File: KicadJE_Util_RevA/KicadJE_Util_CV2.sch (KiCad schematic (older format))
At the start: 53 parts, among them J201 SawOut3, J202 SineOut4, Q201 MMBT3906, Q202 UMX1N, SW201 Octave (3 state), U201 TL072, U202 TL072

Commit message: fix flow
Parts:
- added C? (x2): 1u, Capacitor_SMD:C_1206_3216Metric_Pad1.42x1.75mm_HandSolder, symbol Device:C
- added C? (x4): 100n, Capacitor_SMD:C_0805_2012Metric_Pad1.15x1.40mm_HandSolder, symbol Device:C
- added D? (x10): 1N1007, Diode_SMD:D_SOD-123, symbol Device:D
- added D?: LED, LED_SMD:LED_0805_2012Metric_Pad1.15x1.40mm_HandSolder, symbol Device:LED
- added H? (x4): MountingHole_Pad, AJ:MountingHole_Eurorack3, symbol Mechanical:MountingHole_Pad
- added H?: ON, AJ:LED_Hole_3mm, symbol Mechanical:MountingHole
- added J?: In2.1, AJ-Dropbox-Kicad:PJ301SM, symbol Connector:AudioJack2_SwitchT
- added J?: CV2.1, AJ-Dropbox-Kicad:PJ301SM, symbol Connector:AudioJack2_SwitchT
- added J?: Out2.1, AJ-Dropbox-Kicad:PJ301SM, symbol Connector:AudioJack2_SwitchT
- added J?: CV2.2, AJ-Dropbox-Kicad:PJ301SM, symbol Connector:AudioJack2_SwitchT
- added J?: Out2.2, AJ-Dropbox-Kicad:PJ301SM, symbol Connector:AudioJack2_SwitchT
- added J?: In2.2, AJ-Dropbox-Kicad:PJ301SM, symbol Connector:AudioJack2_SwitchT
- added P?: HEADER_2x5_Doepfer, Connector_IDC:IDC-Header_2x05_P2.54mm_Vertical, symbol Eurorack:HEADER_2x5_Doepfer
- added R? (x10): 10k, Resistor_SMD:R_0805_2012Metric_Pad1.15x1.40mm_HandSolder, symbol Device:R
- added R? (x2): 1k, Resistor_SMD:R_0805_2012Metric_Pad1.15x1.40mm_HandSolder, symbol Device:R
- added R?: 22k, Resistor_SMD:R_0805_2012Metric_Pad1.15x1.40mm_HandSolder, symbol Device:R
- added R? (x2): OPEN, Resistor_SMD:R_0805_2012Metric_Pad1.15x1.40mm_HandSolder, symbol Device:R
- added R?: 100k, Resistor_SMD:R_0805_2012Metric_Pad1.15x1.40mm_HandSolder, symbol Device:R
- added RV?: 100k Offset1, AJ-Dropbox-Kicad:Potentiometer_China_RK09_Single_Vertical_AJ, symbol Envelope-cache-2018-08-04-13-00-04:POT
- added TP?: Tri, AJ:Jack_6m3, symbol Connector:TestPoint
- added TP?: SQ, AJ:Jack_6m3, symbol Connector:TestPoint
- added TP?: SS, AJ:Jack_6m3, symbol Connector:TestPoint
- added TP?: In3, AJ:Jack_6m3, symbol Connector:TestPoint
- added TP?: In2, AJ:Jack_6m3, symbol Connector:TestPoint
- added TP?: In1, AJ:Jack_6m3, symbol Connector:TestPoint
- added TP?: OFF1, AJ:Pot_6m3_scale1, symbol Connector:TestPoint
- added U? (x3): TL072, AJ-Dropbox-Kicad:AJ_SO-8_5.3x6.2mm_P1.27mm, symbol Amplifier_Operational:TL072
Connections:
- net labels added: CV2.1, CV2.2, In2.1, In2.2, Out1, Out2.1, Out2.2
- wire segments 170 -> 319
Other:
- note added: "Power"
- moved on the sheet: C201, C202, C203, C204, C205, D201, J201, J202, JP201, Q201, Q202A, Q202B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

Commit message: Glide initiated
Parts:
- removed C201: 220p, Capacitor_SMD:C_0805_2012Metric_Pad1.15x1.40mm_HandSolder, symbol Device:C
- removed C202, C203: 100n, Capacitor_SMD:C_0805_2012Metric_Pad1.15x1.40mm_HandSolder, symbol Device:C
- removed C204: 1n poly, Capacitor_THT:C_Rect_L7.0mm_W2.0mm_P5.00mm, symbol Device:C
- removed C205: 1n alt, Capacitor_SMD:C_0805_2012Metric_Pad1.15x1.40mm_HandSolder, symbol Device:C
- removed D201: Germanium, Diode_THT:D_A-405_P7.62mm_Horizontal, symbol Device:D
- removed D? (x4): 1N1007, Diode_SMD:D_SOD-123, symbol Device:D
- removed J201: SawOut3, AJ-Dropbox-Kicad:PJ301SM, symbol Connector:AudioJack2_SwitchT
- removed J202: SineOut4, AJ-Dropbox-Kicad:PJ301SM, symbol Connector:AudioJack2_SwitchT
- removed JP201: Jumper_3_Bridged12, Jumper:SolderJumper-3_P1.3mm_Bridged12_Pad1.0x1.5mm_NumberLabels, symbol Jumper:Jumper_3_Bridged12
- removed Q201: MMBT3906, Package_TO_SOT_SMD:SOT-23, symbol Transistor_BJT:MMBT3906
- removed Q202: UMX1N, AJ:UMX1N_UMT6_DualNPN, symbol UMX1N:UMX1N
- removed R201, R203, R225: 47k, Resistor_SMD:R_0805_2012Metric_Pad1.15x1.40mm_HandSolder, symbol Device:R
- removed R202, R218, R234: 1k, Resistor_SMD:R_0805_2012Metric_Pad1.15x1.40mm_HandSolder, symbol Device:R
- removed R204: 1k6, Resistor_SMD:R_0805_2012Metric_Pad1.15x1.40mm_HandSolder, symbol Device:R
- removed R206, R213: 12k5, Resistor_SMD:R_0805_2012Metric_Pad1.15x1.40mm_HandSolder, symbol Device:R
- removed R207: 26k7, Resistor_SMD:R_0805_2012Metric_Pad1.15x1.40mm_HandSolder, symbol Device:R
- removed R208: 6k04, Resistor_SMD:R_0805_2012Metric_Pad1.15x1.40mm_HandSolder, symbol Device:R
- removed R209: 1M2, Resistor_SMD:R_0805_2012Metric_Pad1.15x1.40mm_HandSolder, symbol Device:R
- removed R211: 1k82, Resistor_SMD:R_0805_2012Metric_Pad1.15x1.40mm_HandSolder, symbol Device:R
- removed R212, R216, R221, R227, R230, R? (x5): 10k, Resistor_SMD:R_0805_2012Metric_Pad1.15x1.40mm_HandSolder, symbol Device:R
- removed R217: 3k, Resistor_SMD:R_0805_2012Metric_Pad1.15x1.40mm_HandSolder, symbol Device:R
- removed R219, R222: OPEN, Resistor_SMD:R_0805_2012Metric_Pad1.15x1.40mm_HandSolder, symbol Device:R
- removed R220: 15k, Resistor_SMD:R_0805_2012Metric_Pad1.15x1.40mm_HandSolder, symbol Device:R
- removed R223: 0R, Resistor_SMD:R_0805_2012Metric_Pad1.15x1.40mm_HandSolder, symbol Device:R
- removed R224, R?: 100k, Resistor_SMD:R_0805_2012Metric_Pad1.15x1.40mm_HandSolder, symbol Device:R
- removed R226, R231: 2k20, Resistor_SMD:R_0805_2012Metric_Pad1.15x1.40mm_HandSolder, symbol Device:R
- removed R228: 390R, Resistor_SMD:R_0805_2012Metric_Pad1.15x1.40mm_HandSolder, symbol Device:R
- removed R229: 18k, Resistor_SMD:R_0805_2012Metric_Pad1.15x1.40mm_HandSolder, symbol Device:R
- removed R232, R233: 13k3, Resistor_SMD:R_0805_2012Metric_Pad1.15x1.40mm_HandSolder, symbol Device:R
- removed RV201: 5k, Potentiometer_THT:Potentiometer_Bourns_3296W_Vertical, symbol Device:R_POT_TRIM
- removed RV202: 50k, Potentiometer_THT:Potentiometer_Bourns_3296W_Vertical, symbol Device:R_POT_TRIM
- removed RV?: 100k Offset1, AJ-Dropbox-Kicad:Potentiometer_China_RK09_Single_Vertical_AJ, symbol Envelope-cache-2018-08-04-13-00-04:POT
- removed TP201: Saw, AJ:Jack_6m3, symbol Connector:TestPoint
- removed TP203: 3m5 jack, AJ:Jack_6m3, symbol Connector:TestPoint
- removed TP?: OFF1, AJ:Pot_6m3_scale1, symbol Connector:TestPoint
- removed U201, U202, U?: TL072, AJ-Dropbox-Kicad:AJ_SO-8_5.3x6.2mm_P1.27mm, symbol Amplifier_Operational:TL072
- added C? (x2): 100n, Capacitor_SMD:C_0805_2012Metric_Pad1.15x1.40mm_HandSolder, symbol Device:C
- added D? (x2): LED, LED_THT:LED_D3.0mm, symbol Device:LED
- added R? (x5): 20k, Resistor_SMD:R_0805_2012Metric_Pad1.15x1.40mm_HandSolder, symbol Device:R
- added R? (x2): 220R, Resistor_SMD:R_0805_2012Metric_Pad1.15x1.40mm_HandSolder, symbol Device:R
- added R? (x2): OPEN, Resistor_SMD:R_0805_2012Metric_Pad1.15x1.40mm_HandSolder, symbol Device:R
- added R? (x2): 1k, Resistor_SMD:R_0805_2012Metric_Pad1.15x1.40mm_HandSolder, symbol Device:R
- added R?: 10k, Resistor_SMD:R_0805_2012Metric_Pad1.15x1.40mm_HandSolder, symbol Device:R
- added R?: LDR03, OptoDevice:R_LDR_10x8.5mm_P7.6mm_Vertical, symbol Sensor_Optical:LDR03
- added RV?: 100k Glide1, AJ-Dropbox-Kicad:Potentiometer_China_RK09_Single_Vertical_AJ, symbol Envelope-cache-2018-08-04-13-00-04:POT
- added RV?: 100k Glide2, AJ-Dropbox-Kicad:Potentiometer_China_RK09_Single_Vertical_AJ, symbol Envelope-cache-2018-08-04-13-00-04:POT
- added TP?: Glide2, AJ:Pot_6m3_scale1, symbol Connector:TestPoint
- added TP?: Glide1, AJ:Pot_6m3_scale1, symbol Connector:TestPoint
- added TP?: Flow1, TestPoint:TestPoint_THTPad_2.0x2.0mm_Drill1.0mm, symbol Connector:TestPoint
- added TP?: Flow2, TestPoint:TestPoint_THTPad_2.0x2.0mm_Drill1.0mm, symbol Connector:TestPoint
- added U? (x2): TL072, AJ-Dropbox-Kicad:AJ_SO-8_5.3x6.2mm_P1.27mm, symbol Amplifier_Operational:TL072
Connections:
- net labels removed: -5V, 3CVIn1, 3FM_Lin_In4, 3HardSyncIn3, 3PWM_In5, 3Sine, 3SoftSyncIn2, 3VP_2, 3VSO_3, 3VTO_1, CV2.1, CV2.2, Out1
- wire segments 319 -> 198
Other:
- note added: "INCOMPLETE !!!\n\nThink it through"
- note added: "NonInv/Inv Input"
- note added: "Output"
- note removed: "1n timing cap\n0805 as backup\nTHT 1000 pf poly"
- note removed: "Prophet 5"
- note removed: "Prophet T8"
- moved on the sheet: R205, R210, R214, R215, SW201, TP202

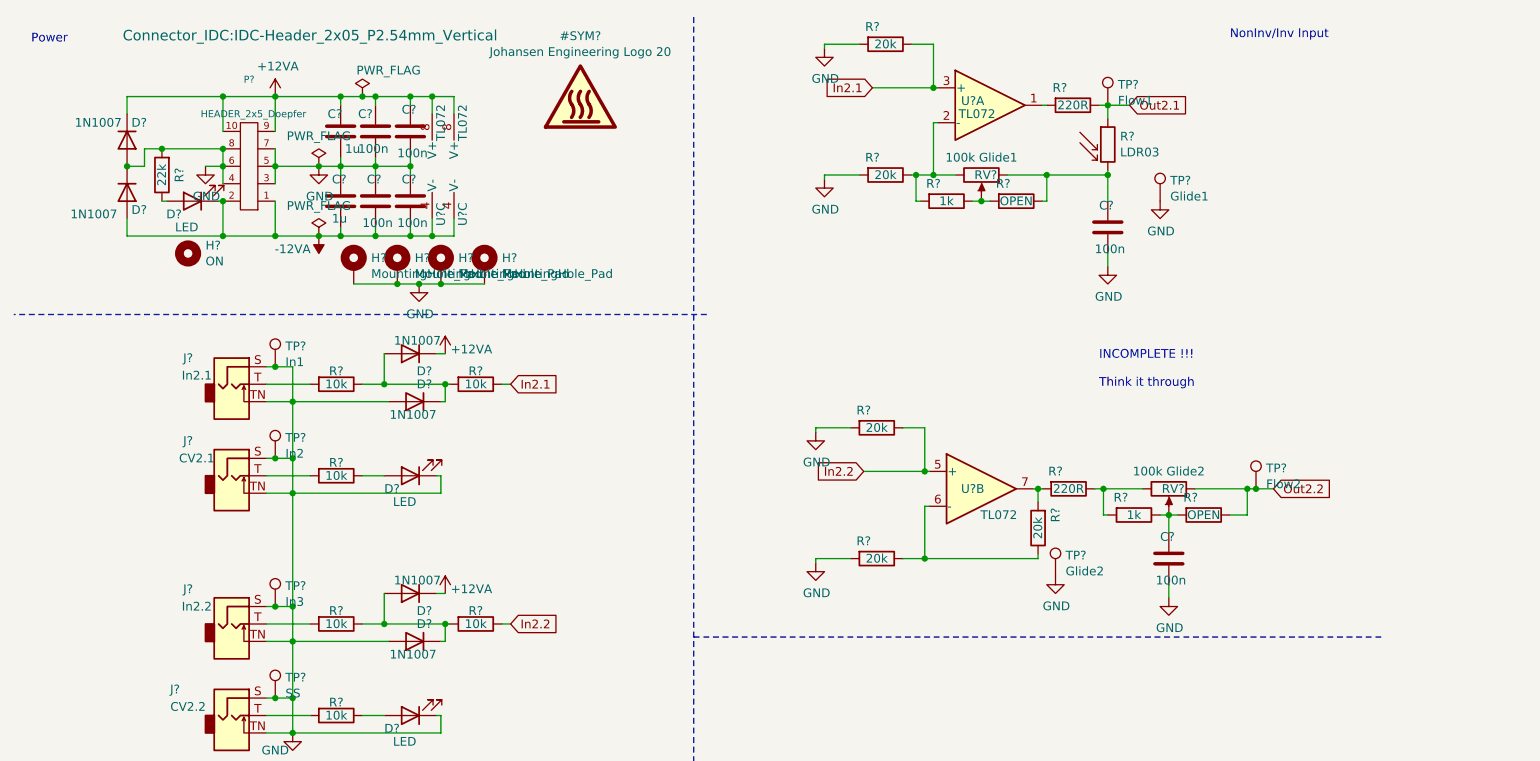
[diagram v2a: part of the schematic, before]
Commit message: Update KicadJE_Util_CV2.sch
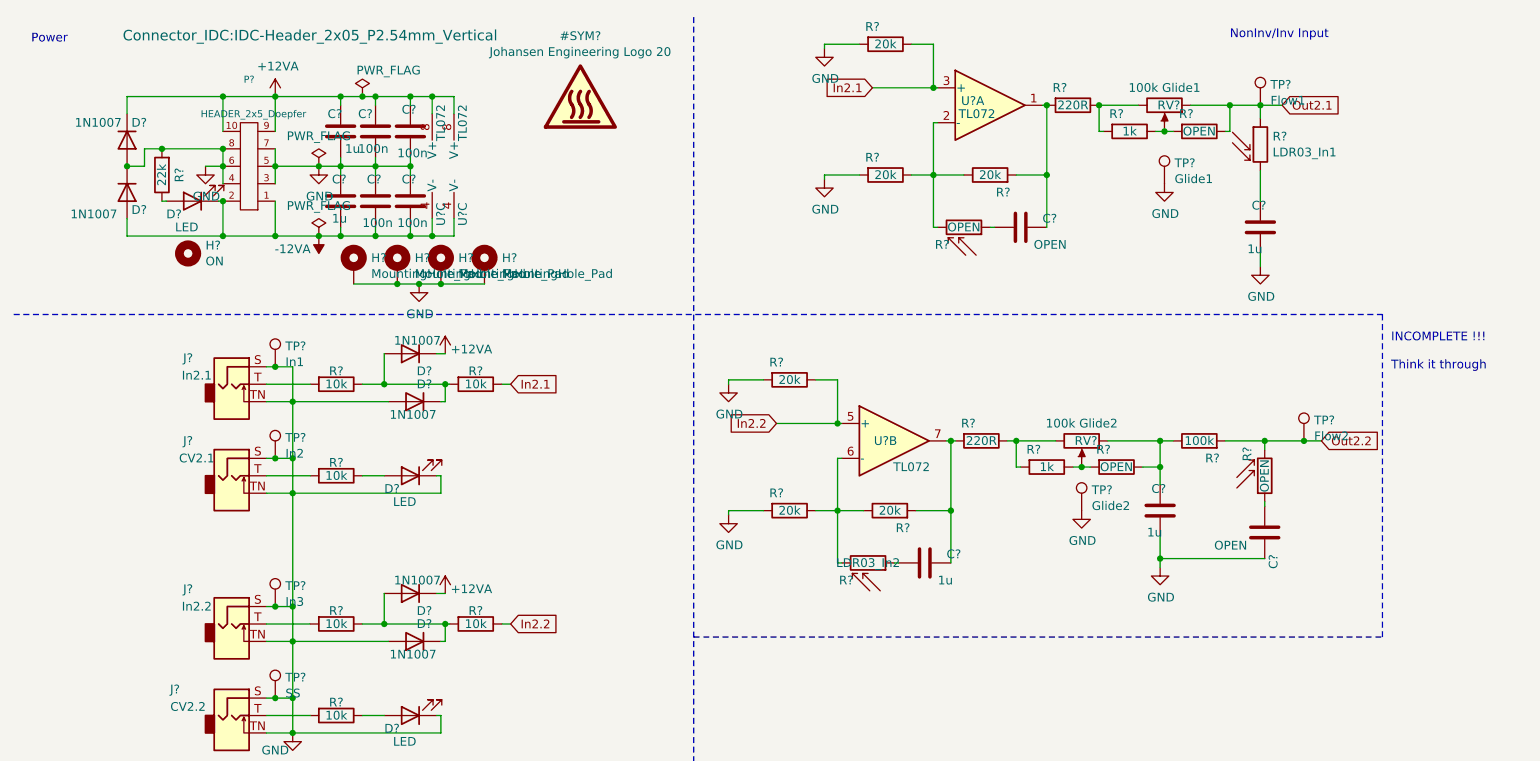
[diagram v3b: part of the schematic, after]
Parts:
- removed R?: 20k, Resistor_SMD:R_0805_2012Metric_Pad1.15x1.40mm_HandSolder, symbol Device:R
- added C? (x2): OPEN, Capacitor_SMD:C_0805_2012Metric_Pad1.15x1.40mm_HandSolder, symbol Device:C
- added C?: 1u, Capacitor_SMD:C_0805_2012Metric_Pad1.15x1.40mm_HandSolder, symbol Device:C
- added R? (x2): 20k, Resistor_SMD:R_0805_2012Metric_Pad1.15x1.40mm_HandSolder, symbol Device:R
- added R? (x2): OPEN, OptoDevice:R_LDR_10x8.5mm_P7.6mm_Vertical, symbol Sensor_Optical:LDR03
- added R?: 100k, Resistor_SMD:R_0805_2012Metric_Pad1.15x1.40mm_HandSolder, symbol Device:R
- added R?: LDR03_In2, OptoDevice:R_LDR_10x8.5mm_P7.6mm_Vertical, symbol Sensor_Optical:LDR03
- C? (x2): value 100n -> 1u
- R?: value LDR03 -> LDR03_In1
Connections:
- net GND: now also C?.1
- net Out2.1: now also R?.1, RV?.1; no longer R?.1
- net Out2.2: now also R?.2, R?.2; no longer R?.1, RV?.1
- net at R?.2, U?.1: now also C?.1, R?.2
- net at R?.1, U?.2 (-): now also R?.1, R?.2; no longer R?.2, RV?.3
- net at R?.1, U?.6 (-): now also R?.1, R?.2
- net at R?.2, U?.7: now also C?.1, R?.2
- net at C?.1, R?.2: no longer R?.1, RV?.1
- net at R?.1, R?.2, RV?.2: no longer C?.1
- new net: R?.1, R?.2, RV?.3
- new net: C?.1, R?.1, R?.1, RV?.1
- new net: C?.2, R?.1 (x3)
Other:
- moved on the sheet: C?, R?, RV?, TP?, U?B

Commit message: Update KicadJE_Util_CV2.sch
Glide
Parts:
- added C?: 1u, Capacitor_SMD:C_0805_2012Metric_Pad1.15x1.40mm_HandSolder, symbol Device:C
- added R?: 20k, Resistor_SMD:R_0805_2012Metric_Pad1.15x1.40mm_HandSolder, symbol Device:R
- added U? (x2): TL072, AJ-Dropbox-Kicad:AJ_SO-8_5.3x6.2mm_P1.27mm, symbol Amplifier_Operational:TL072
- C?: value 1u -> 4u7
- R?: value 100k -> 20k
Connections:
- net GND: now also C?.2
- net In2.1: now also U?.5 (+); no longer U?.3 (+)
- net Out2.1: now also U?.3 (+), R?.1; no longer R?.1, R?.1, RV?.1
- net Out2.2: now also U?.3 (+); no longer R?.1
- net at C?.1, R?.2, R?.2: now also U?.7; no longer U?.1
- net at R?.1, R?.1, R?.2: now also U?.6 (-); no longer U?.2 (-)
- new net: R?.1, U?.1, U?.2 (-) (x2)
- new net: C?.1, R?.1, R?.2, RV?.1
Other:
- note removed: "INCOMPLETE !!!\n\nThink it through"
- moved on the sheet: C?, R?, RV?, TP?, U?A

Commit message: Timeshift Added
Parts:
- removed R205: 47k, Resistor_SMD:R_0805_2012Metric_Pad1.15x1.40mm_HandSolder, symbol Device:R
- removed R210: 470R, Resistor_SMD:R_0805_2012Metric_Pad1.15x1.40mm_HandSolder, symbol Device:R
- removed R214: 82k, Resistor_SMD:R_0805_2012Metric_Pad1.15x1.40mm_HandSolder, symbol Device:R
- removed R215: 20k, Resistor_SMD:R_0805_2012Metric_Pad1.15x1.40mm_HandSolder, symbol Device:R
- removed SW201: Octave (3 state), AJ-Dropbox-Kicad:SP1MS1, symbol Switch:SW_SPDT
- removed TP202: Oct, AJ:Pot_6m3, symbol Connector:TestPoint
- R? (x4): value 1k -> 680R
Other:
- note removed: "Octave Adjust"

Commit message: annotate
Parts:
- gave numbers to parts that had none: 76

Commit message: ERC
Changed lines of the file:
@@
 Wire Wire Line
 	2450 1050 2450 1000
-Connection ~ 2575 1000
-Wire Wire Line
-	2575 1000 2650 1000
-$Comp
-L power:PWR_FLAG #FLG?
-U 1 1 5E7BA41B
-P 2575 1000
-AR Path="/5E4B0DD9/5E7BA41B" Ref="#FLG?"  Part="1"
-AR Path="/5E62ACA1/5E7BA41B" Ref="#FLG?"  Part="1"
-AR Path="/5F49A670/5E7BA41B" Ref="#FLG?"  Part="1"
-AR Path="/5E7BA41B" Ref="#FLG?"  Part="1"
-AR Path="/5FDBD837/5E7BA41B" Ref="#FLG0203"  Part="1"
-F 0 "#FLG0203" H 2575 1075 50  0001 C CNN
-F 1 "PWR_FLAG" H 2725 1150 50  0000 C CNN
-F 2 "" H 2575 1000 50  0001 C CNN
-F 3 "~" H 2575 1000 50  0001 C CNN
-	1    2575 1000
-	1    0    0    -1
-$EndComp
-$Comp
-L power:PWR_FLAG #FLG?
-U 1 1 5E7BA421
-P 2325 1400
-AR Path="/5E4B0DD9/5E7BA421" Ref="#FLG?"  Part="1"
-AR Path="/5E62ACA1/5E7BA421" Ref="#FLG?"  Part="1"
-AR Path="/5F49A670/5E7BA421" Ref="#FLG?"  Part="1"
-AR Path="/5E7BA421" Ref="#FLG?"  Part="1"
-AR Path="/5FDBD837/5E7BA421" Ref="#FLG0201"  Part="1"
-F 0 "#FLG0201" H 2325 1475 50  0001 C CNN
-F 1 "PWR_FLAG" H 2325 1573 50  0000 C CNN
-F 2 "" H 2325 1400 50  0001 C CNN
-F 3 "~" H 2325 1400 50  0001 C CNN
-	1    2325 1400
-	1    0    0    -1
-$EndComp
-$Comp
-L power:PWR_FLAG #FLG?
-U 1 1 5E7BA427
-P 2325 1800
-AR Path="/5E4B0DD9/5E7BA427" Ref="#FLG?"  Part="1"
-AR Path="/5E62ACA1/5E7BA427" Ref="#FLG?"  Part="1"
-AR Path="/5F49A670/5E7BA427" Ref="#FLG?"  Part="1"
-AR Path="/5E7BA427" Ref="#FLG?"  Part="1"
-AR Path="/5FDBD837/5E7BA427" Ref="#FLG0202"  Part="1"
-F 0 "#FLG0202" H 2325 1875 50  0001 C CNN
-F 1 "PWR_FLAG" H 2325 1973 50  0000 C CNN
-F 2 "" H 2325 1800 50  0001 C CNN
-F 3 "~" H 2325 1800 50  0001 C CNN
-	1    2325 1800
-	1    0    0    -1
-$EndComp
 $Comp
 L Envelope-cache-2018-08-04-13-00-04:GND #PWR?
@@
 	2450 1800 2650 1800
 Connection ~ 2450 1000
-Wire Wire Line
-	2450 1000 2575 1000
 Wire Wire Line
 	2450 1400 2650 1400
@@
 	2425 5325 2775 5325
 Connection ~ 2775 5325
+Wire Wire Line
+	2450 1000 2650 1000
 $EndSCHEMATC

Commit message: Labels and DRC
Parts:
- R216, R217, R228, R229: footprint OptoDevice:R_LDR_10x8.5mm_P7.6mm_Vertical -> OptoDevice:R_LDR_5.0x4.1mm_P3mm_Vertical
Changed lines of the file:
@@
 F 0 "R228" H 7720 1421 50  0000 L CNN
 F 1 "LDR03_In1" H 7720 1330 50  0000 L CNN
-F 2 "OptoDevice:R_LDR_10x8.5mm_P7.6mm_Vertical" V 7825 1375 50  0001 C CNN
+F 2 "OptoDevice:R_LDR_5.0x4.1mm_P3mm_Vertical" V 7825 1375 50  0001 C CNN
 F 3 "http://www.elektronica-componenten.nl/WebRoot/StoreNL/Shops/61422969/54F1/BA0C/C664/31B9/2173/C0A8/2AB9/2AEF/LDR03IMP.pdf" H 7650 1325 50  0001 C CNN
 	1    7650 1375
@@
 F 0 "R229" V 7650 3050 50  0000 C CNN
 F 1 "OPEN" V 7750 3175 50  0000 C CNN
-F 2 "OptoDevice:R_LDR_10x8.5mm_P7.6mm_Vertical" V 7925 3175 50  0001 C CNN
+F 2 "OptoDevice:R_LDR_5.0x4.1mm_P3mm_Vertical" V 7925 3175 50  0001 C CNN
 F 3 "http://www.elektronica-componenten.nl/WebRoot/StoreNL/Shops/61422969/54F1/BA0C/C664/31B9/2173/C0A8/2AB9/2AEF/LDR03IMP.pdf" H 7750 3125 50  0001 C CNN
 	1    7750 3175
@@
 F 0 "R216" V 5375 1725 50  0000 C CNN
 F 1 "OPEN" V 5475 1850 50  0000 C CNN
-F 2 "OptoDevice:R_LDR_10x8.5mm_P7.6mm_Vertical" V 5650 1850 50  0001 C CNN
+F 2 "OptoDevice:R_LDR_5.0x4.1mm_P3mm_Vertical" V 5650 1850 50  0001 C CNN
 F 3 "http://www.elektronica-componenten.nl/WebRoot/StoreNL/Shops/61422969/54F1/BA0C/C664/31B9/2173/C0A8/2AB9/2AEF/LDR03IMP.pdf" H 5475 1800 50  0001 C CNN
 	1    5475 1850
@@
 F 0 "R217" V 5375 3550 50  0000 C CNN
 F 1 "LDR03_In2" V 5475 3675 50  0000 C CNN
-F 2 "OptoDevice:R_LDR_10x8.5mm_P7.6mm_Vertical" V 5650 3675 50  0001 C CNN
+F 2 "OptoDevice:R_LDR_5.0x4.1mm_P3mm_Vertical" V 5650 3675 50  0001 C CNN
 F 3 "http://www.elektronica-componenten.nl/WebRoot/StoreNL/Shops/61422969/54F1/BA0C/C664/31B9/2173/C0A8/2AB9/2AEF/LDR03IMP.pdf" H 5475 3625 50  0001 C CNN
 	1    5475 3675
